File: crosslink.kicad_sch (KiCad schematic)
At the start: 34 parts, among them U16 CrossLink_LIF-MD6000-6JMG80I

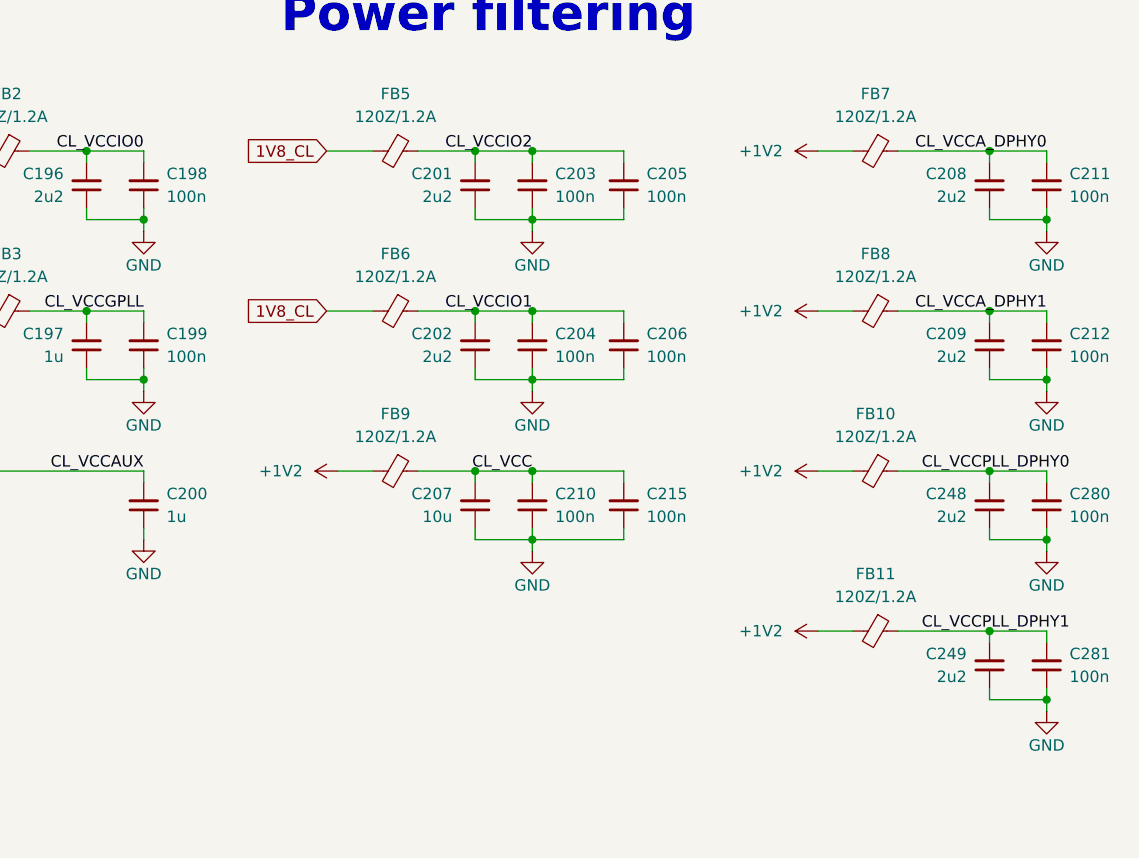
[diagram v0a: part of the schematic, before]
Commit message: [#55992] Replace 100n capacitors
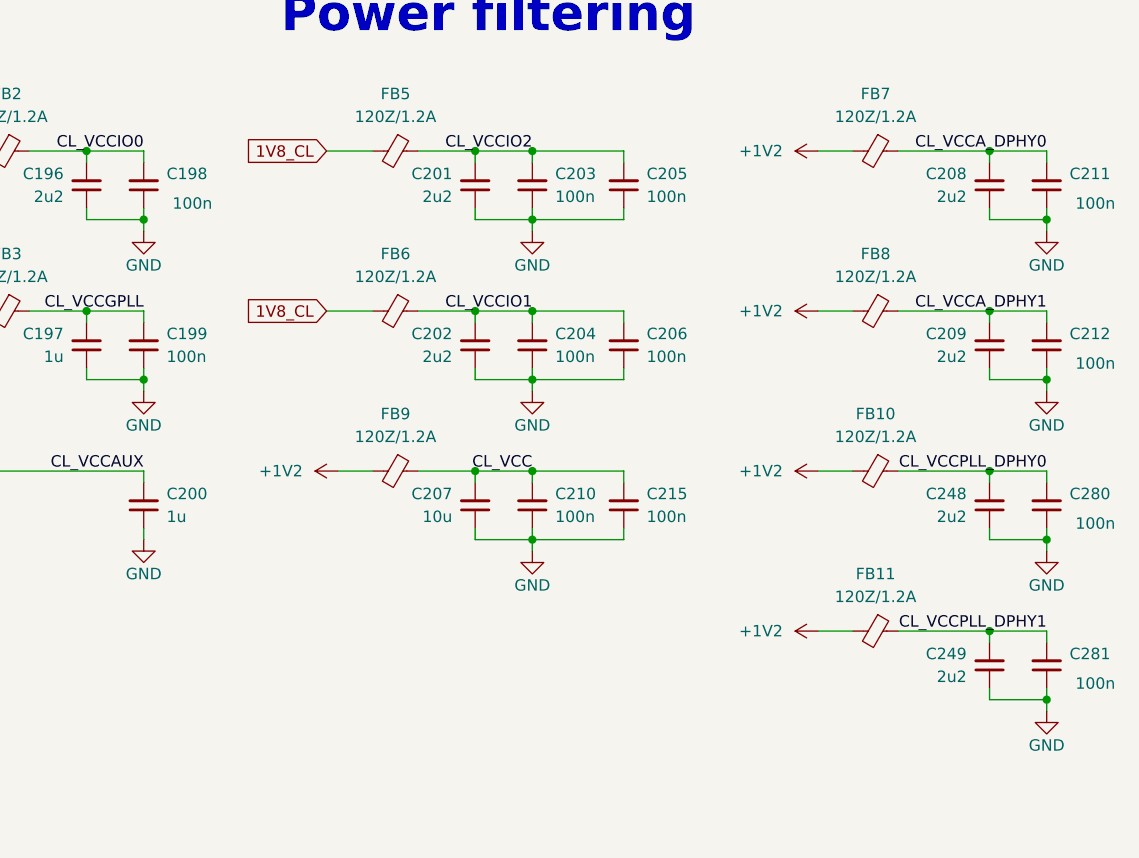
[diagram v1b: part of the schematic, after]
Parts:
- C198, C199, C203, C204, C205, C206, C210, C211, C212, C215, C280, C281: value C_100n_0201_25V -> C_100n_0402; footprint antmicro-footprints:C_0201 -> antmicro-footprints:C_0402_1005Metric; symbol antmicroCapacitorsmisc:C_100n_0201_25V -> antmicroCapacitors0402:C_100n_0402; MPN C0603X5R1E104K030BB -> GRM155R61H104KE14D; Manufacturer TDK -> Murata; Voltage 25V -> 50V
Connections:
- net CL_VCCPLL_DPHY0: now also C248.2, C280.2, FB10.1
- net CL_VCCPLL_DPHY1: now also C249.2, C281.2, FB11.1

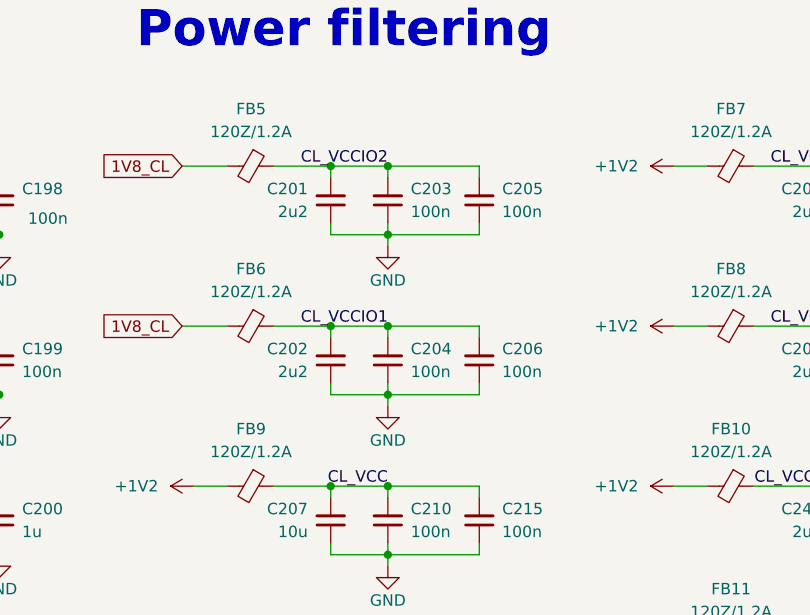
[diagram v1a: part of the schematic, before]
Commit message: [#56060] Reduce decoupling
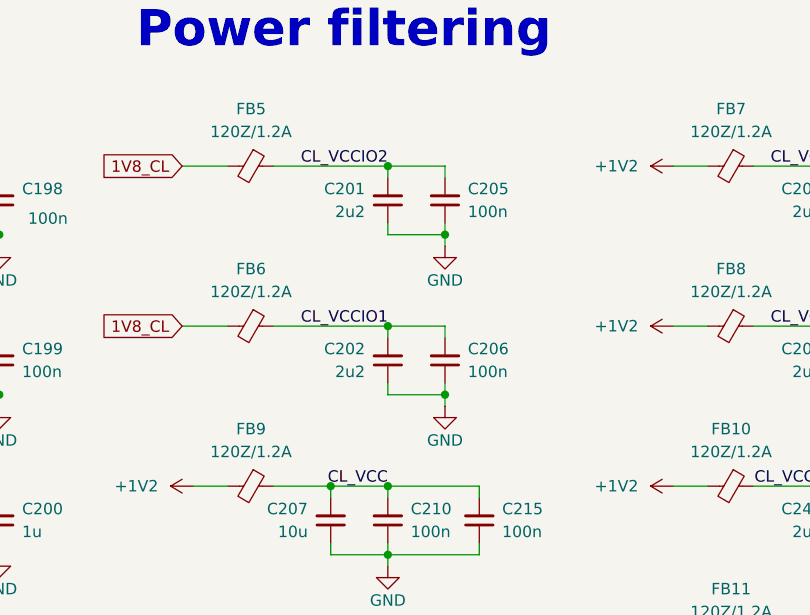
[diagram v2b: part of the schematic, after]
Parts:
- removed C203, C204: C_100n_0402, antmicro-footprints:C_0402_1005Metric, symbol antmicroCapacitors0402:C_100n_0402
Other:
- moved on the sheet: C201, C202, C205, C206

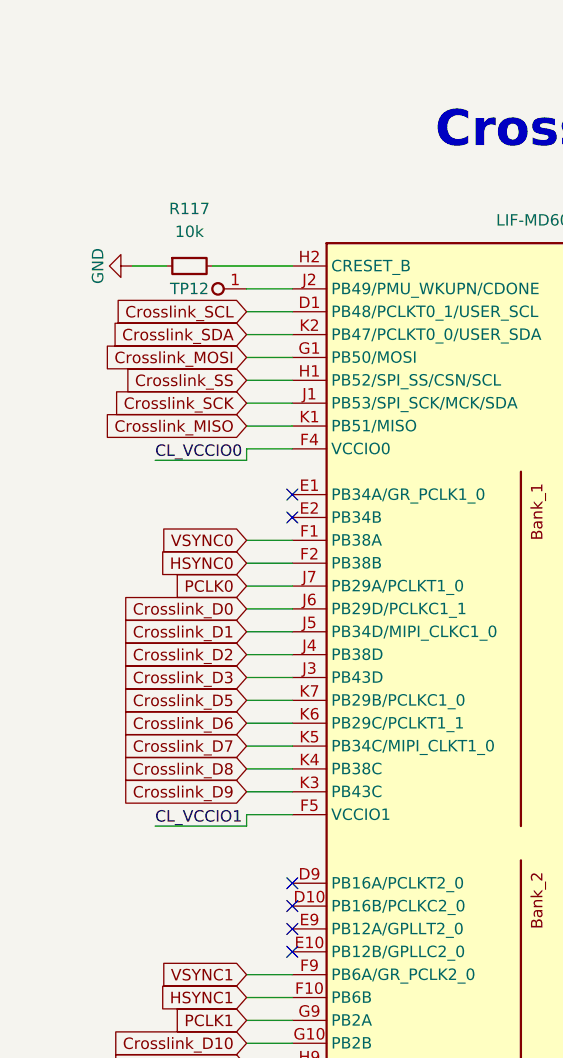
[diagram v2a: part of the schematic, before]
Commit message: [#56466] Update CrossLink's connection
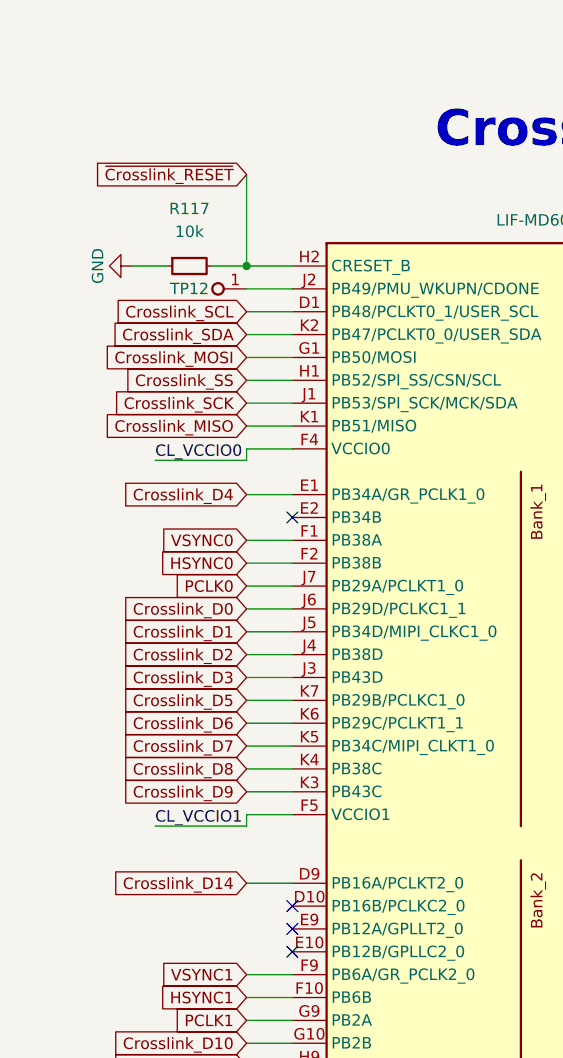
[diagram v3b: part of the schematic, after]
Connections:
- net ~{Crosslink_RESET}: now reaches R117.2, U16.H2 (CRESET_B)
- net Crosslink_D14: now reaches U16.D9 (PB16A/PCLKT2_0)
- net Crosslink_D4: now reaches U16.E1 (PB34A/GR_PCLK1_0)
- no-connect marks 6 -> 4
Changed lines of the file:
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@@
   (junction (at 361.95 137.16) (diameter 0) (color 0 0 0 0)
   )
+  (junction (at 81.28 80.01) (diameter 0) (color 0 0 0 0)
+  )
   (junction (at 355.6 147.32) (diameter 0) (color 0 0 0 0)
   )
@@
   (junction (at 355.6 111.76) (diameter 0) (color 0 0 0 0)
   )
-  (no_connect (at 86.36 148.59))
   (no_connect (at 86.36 151.13))
   (no_connect (at 86.36 156.21))
-  (no_connect (at 86.36 105.41))
   (no_connect (at 86.36 107.95))
   (no_connect (at 86.36 153.67))
@@
     (stroke (width 0) (type default))
   )
+  (wire (pts (xy 81.28 69.85) (xy 81.28 80.01))
+    (stroke (width 0) (type default))
+  )
   (wire (pts (xy 149.86 138.43) (xy 154.94 138.43))
     (stroke (width 0) (type default))
@@
     (stroke (width 0) (type default))
   )
+  (wire (pts (xy 81.28 148.59) (xy 86.36 148.59))
+    (stroke (width 0) (type default))
+  )
   (wire (pts (xy 149.86 184.15) (xy 153.67 184.15))
     (stroke (width 0) (type default))
@@
     (stroke (width 0) (type default))
   )
-  (wire (pts (xy 86.36 80.01) (xy 77.47 80.01))
+  (wire (pts (xy 86.36 80.01) (xy 81.28 80.01))
     (stroke (width 0) (type default))
   )
@@
     (stroke (width 0) (type default))
   )
+  (wire (pts (xy 81.28 105.41) (xy 86.36 105.41))
+    (stroke (width 0) (type default))
+  )
   (wire (pts (xy 361.95 147.32) (xy 361.95 148.59))
     (stroke (width 0) (type default))
@@
   )
   (wire (pts (xy 304.8 93.98) (xy 311.15 93.98))
+    (stroke (width 0) (type default))
+  )
+  (wire (pts (xy 81.28 80.01) (xy 77.47 80.01))
     (stroke (width 0) (type default))
   )
@@
     )
   )
+  (global_label "Crosslink_D4" (shape input) (at 81.28 105.41 180) (fields_autoplaced)
+    (effects (font (size 1.27 1.27)) (justify right))
+    (property "Intersheetrefs" "${INTERSHEET_REFS}" (at 66.1392 105.41 0)
+      (effects (font (size 1.27 1.27)) (justify right) hide)
+    )
+  )
   (global_label "CAM1_D0_P" (shape input) (at 154.94 100.33 0) (fields_autoplaced)
     (effects (font (size 1.27 1.27)) (justify left))
@@
     )
   )
+  (global_label "Crosslink_D14" (shape input) (at 81.28 148.59 180) (fields_autoplaced)
+    (effects (font (size 1.27 1.27)) (justify right))
+    (property "Intersheetrefs" "${INTERSHEET_REFS}" (at 64.9297 148.59 0)
+      (effects (font (size 1.27 1.27)) (justify right) hide)
+    )
+  )
   (global_label "VSYNC1" (shape input) (at 81.28 158.75 180) (fields_autoplaced)
     (effects (font (size 1.27 1.27)) (justify right))
@@
       (effects (font (size 1.27 1.27)) (justify right) hide)
     )
+  )
+  (global_label "~{Crosslink_RESET}" (shape input) (at 81.28 69.85 180) (fields_autoplaced)
+    (effects (font (size 1.27 1.27)) (justify right))
+    (property "Intersheetrefs" "${INTERSHEET_REFS}" (at 62.8736 69.85 0)
+      (effects (font (size 1.27 1.27)) (justify right) hide)
+    )

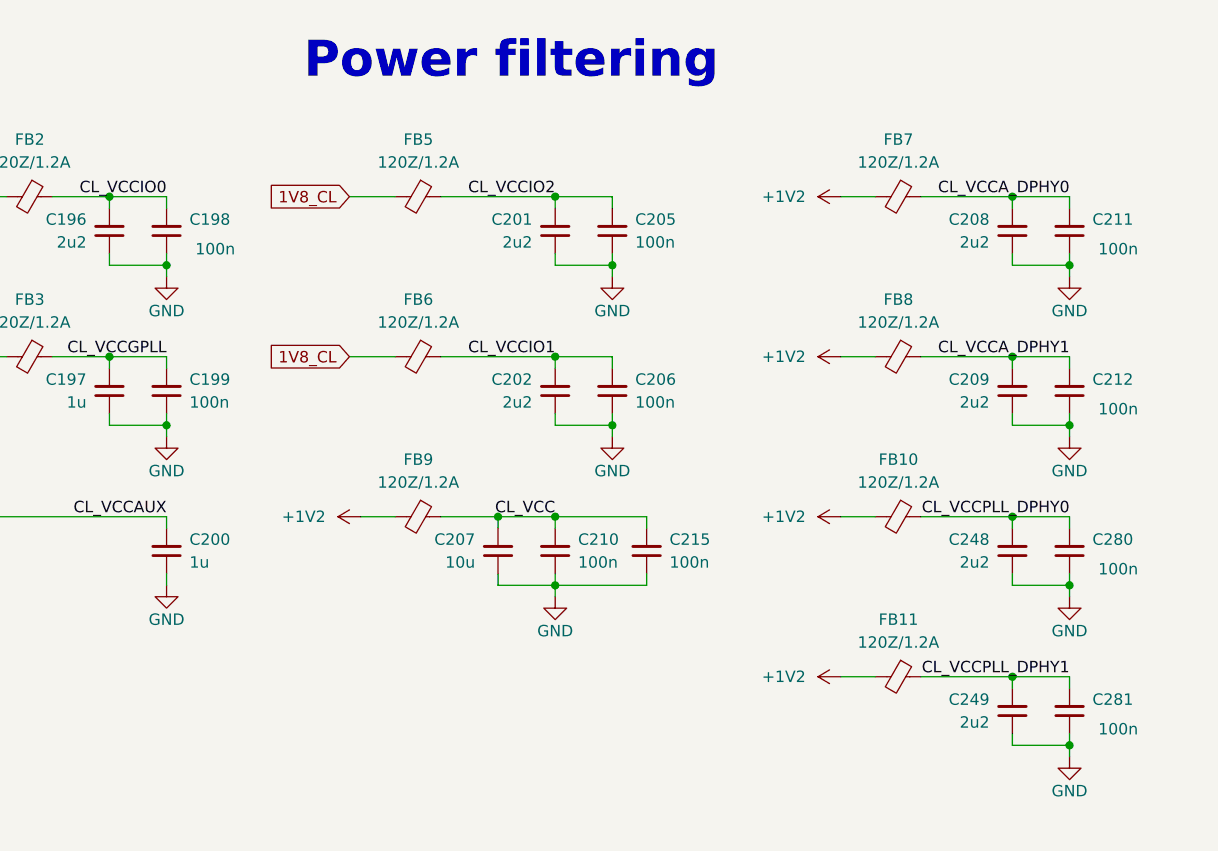
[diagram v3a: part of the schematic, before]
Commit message: [#56952] Place top designators, clean ERC
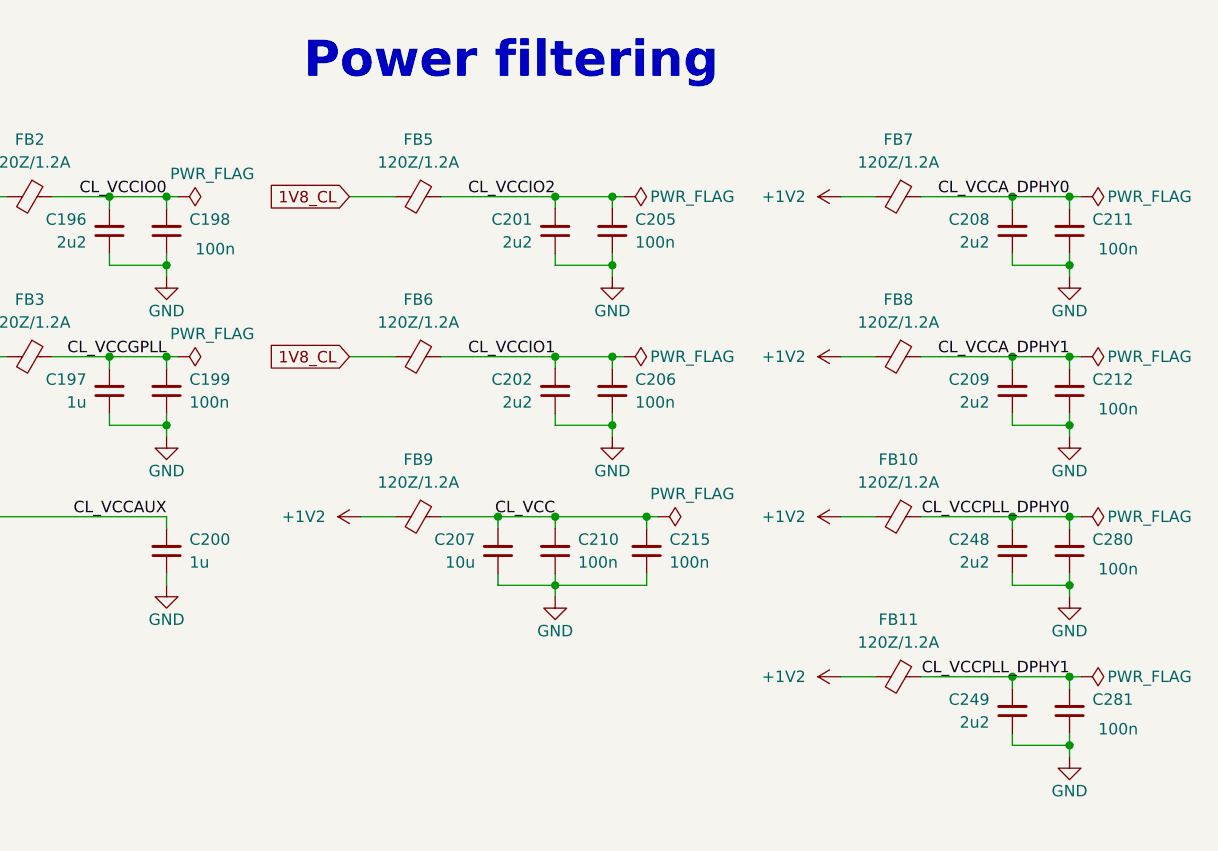
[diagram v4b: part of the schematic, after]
